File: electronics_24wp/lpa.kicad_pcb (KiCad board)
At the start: 2 copper layers, 143 x 74 mm, 89 parts, among them IC1 ATMEGA328-A, P1 CONN_2, P2 CONN_3X2, U1 SD_CARD, U2 LD1117S33, U3 TLC5941, U4 TLC5941, U5 TLC5941, X1 CRYSTAL_SMD

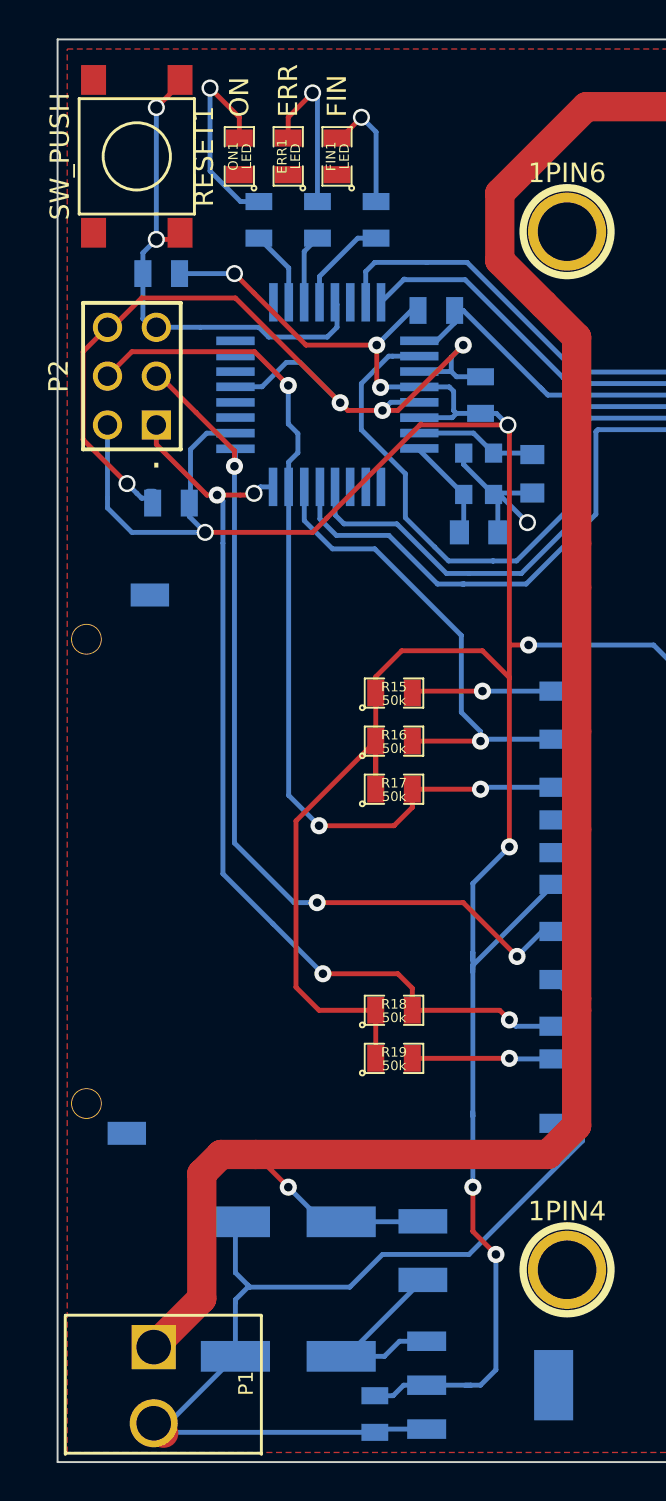
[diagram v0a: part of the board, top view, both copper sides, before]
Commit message: Streamlined layout libraries.
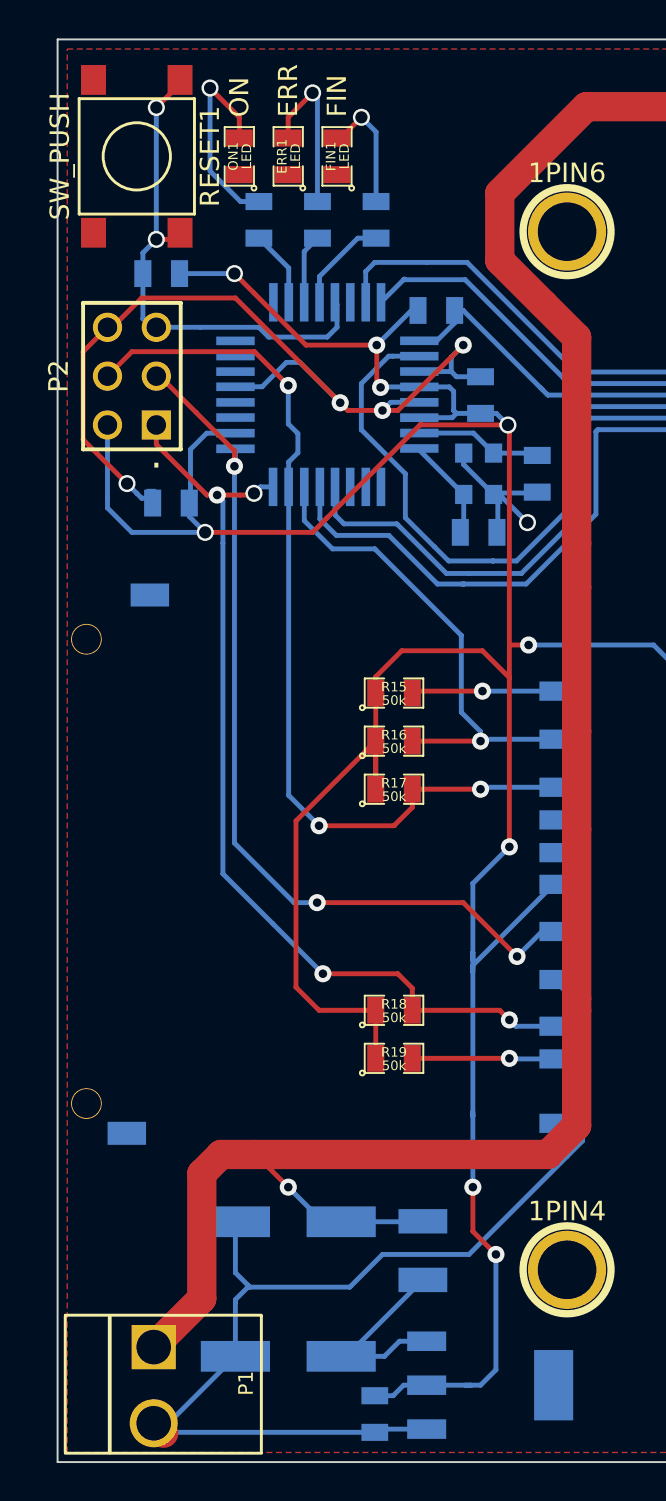
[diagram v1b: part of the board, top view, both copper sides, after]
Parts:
- C1, C2, C5, C6, C7, C8, ERR1, FIN1, ON1, R1, R15, R16, R17, R18, R19, R2, R3, R4, R5, R_ERR1, R_FIN1, R_ON1: footprint SM0805 -> LPA_parts:SM0805
- C10, C9: footprint Capacitors_SMD:C_0805 -> LPA_parts:SM0805
- D1, D10, D11, D12, D13, D14, D15, D16, D17, D18, D19, D2, D20, D21, D22, D23, D24, D25, D26, D27, D28, D29, D3, D30, D31, D32, D33, D34, D35, D36, D37, D38, D39, D4, D40, D41, D42, D43, D44, D45, D46, D47, D48, D5, D6, D7, D8, D9: footprint LPA_parts:PCV220_LEDSOCKET -> LPA_parts:PCV220_LED_SOCKET
- IC1: footprint TQFP32_FIXED -> LPA_parts:ATMEGA328
- P1: footprint PIN_ARRAY_2X1_3960um -> LPA_parts:CONNECTOR_2X1_3960um
- RESET1: footprint SW_PUSH_SMD -> LPA_parts:SW_PUSH_SMD
- U1: footprint SD_CONN -> LPA_parts:SD_CARD_SOCKET
- U3, U4, U5: footprint LPA_parts:TLC5940_THERMVIAS -> LPA_parts:TLC5941
- X1: footprint LPA_parts:Crystal_SMD_3.2_2.5_4pins -> LPA_parts:CRYSTAL_SMD_3.2_2.5_4pins
- moved C9 0.25 mm to (91.9, 117.1)

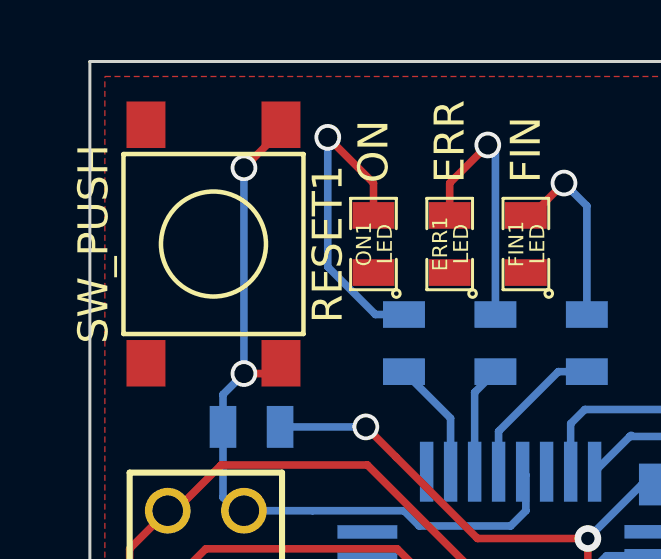
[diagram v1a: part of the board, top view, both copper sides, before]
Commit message: Changed reset button layout for standard library item.
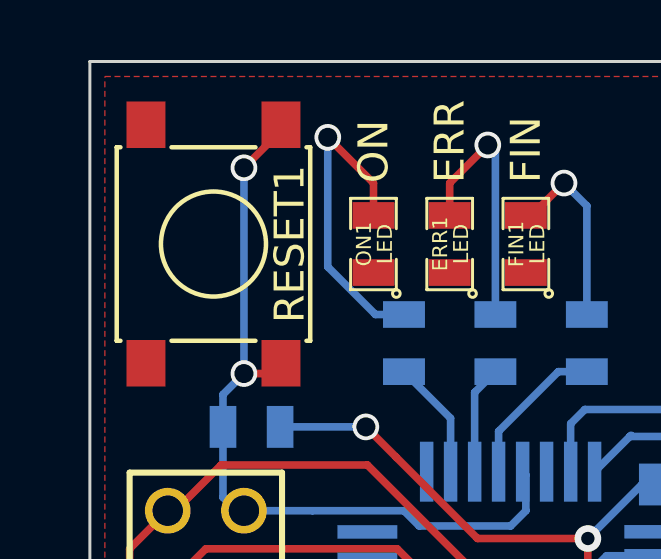
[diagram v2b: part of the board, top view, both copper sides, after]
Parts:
- RESET1: footprint LPA_parts:SW_PUSH_SMD -> Buttons_Switches_SMD:SW_SPST_PTS645
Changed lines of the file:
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@@
     (pad H thru_hole circle (at 0 -12.85 180) (size 1.6 1.6) (drill 1.5) (layers *.Cu *.Mask B.SilkS))
-  )
-  (module LPA_parts:SW_PUSH_SMD (layer F.Cu)
-    (at 71.12 100.584 270)
-    (fp_text reference RESET1 (at 0 -3.81 270) (layer F.SilkS)
-      (effects (font (size 1 1) (thickness 0.15)))
-    )
-    (fp_text value SW_PUSH (at 0 4 270) (layer F.SilkS)
-      (effects (font (size 1 1) (thickness 0.15)))
-    )
-    (fp_circle (center 0 0) (end 1.75 0) (layer F.SilkS) (width 0.15))
-    (fp_line (start -3 -3) (end -3 3) (layer F.SilkS) (width 0.15))
-    (fp_line (start -3 3) (end 3 3) (layer F.SilkS) (width 0.15))
-    (fp_line (start 3 3) (end 3 -3) (layer F.SilkS) (width 0.15))
-    (fp_line (start 3 -3) (end -3 -3) (layer F.SilkS) (width 0.15))
-    (pad 1 smd rect (at 3.975 -2.25 270) (size 1.55 1.3) (layers F.Cu F.Paste F.Mask)
-      (net 6 /RST))
-    (pad 2 smd rect (at 3.975 2.25 270) (size 1.55 1.3) (layers F.Cu F.Paste F.Mask)
-      (net 17 GND))
-    (pad 2 smd rect (at -3.975 2.25 270) (size 1.55 1.3) (layers F.Cu F.Paste F.Mask)
-      (net 17 GND))
-    (pad 1 smd rect (at -3.975 -2.25 270) (size 1.55 1.3) (layers F.Cu F.Paste F.Mask)
-      (net 6 /RST))
   )
   (module LPA_parts:CONNECTOR_2X1_3960um (layer F.Cu)
@@
     )
   )
+  (module Buttons_Switches_SMD:SW_SPST_PTS645 (layer F.Cu)
+    (at 71.12 100.584 270)
+    (descr "C&K Components SPST SMD PTS645 Series 6mm Tact Switch")
+    (tags "SPST Button Switch")
+    (fp_text reference RESET1 (at 0 -2.54 270) (layer F.SilkS)
+      (effects (font (size 1 1) (thickness 0.15)))
+    )
+    (fp_text value SW_PUSH (at 0 4.064 270) (layer F.Fab)
+      (effects (font (size 1 1) (thickness 0.15)))
+    )
+    (fp_circle (center 0 0) (end 1.75 -0.05) (layer F.SilkS) (width 0.15))
+    (fp_line (start 5.05 3.4) (end 5.05 -3.4) (layer F.CrtYd) (width 0.05))
+    (fp_line (start -5.05 -3.4) (end -5.05 3.4) (layer F.CrtYd) (width 0.05))
+    (fp_line (start -5.05 3.4) (end 5.05 3.4) (layer F.CrtYd) (width 0.05))
+    (fp_line (start -5.05 -3.4) (end 5.05 -3.4) (layer F.CrtYd) (width 0.05))
+    (fp_line (start 3.225 -3.225) (end 3.225 -3.1) (layer F.SilkS) (width 0.15))
+    (fp_line (start 3.225 3.225) (end 3.225 3.1) (layer F.SilkS) (width 0.15))
+    (fp_line (start -3.225 3.225) (end -3.225 3.1) (layer F.SilkS) (width 0.15))
+    (fp_line (start -3.225 -3.1) (end -3.225 -3.225) (layer F.SilkS) (width 0.15))
+    (fp_line (start 3.225 -1.4) (end 3.225 1.4) (layer F.SilkS) (width 0.15))
+    (fp_line (start -3.225 -3.225) (end 3.225 -3.225) (layer F.SilkS) (width 0.15))
+    (fp_line (start -3.225 -1.4) (end -3.225 1.4) (layer F.SilkS) (width 0.15))
+    (fp_line (start -3.225 3.225) (end 3.225 3.225) (layer F.SilkS) (width 0.15))
+    (pad 2 smd rect (at -3.975 2.25 270) (size 1.55 1.3) (layers F.Cu F.Paste F.Mask)
+      (net 17 GND))
+    (pad 1 smd rect (at -3.975 -2.25 270) (size 1.55 1.3) (layers F.Cu F.Paste F.Mask)
+      (net 6 /RST))
+    (pad 1 smd rect (at 3.975 -2.25 270) (size 1.55 1.3) (layers F.Cu F.Paste F.Mask)
+      (net 6 /RST))
+    (pad 2 smd rect (at 3.975 2.25 270) (size 1.55 1.3) (layers F.Cu F.Paste F.Mask)
+      (net 17 GND))
+  )
   (gr_text . (at 72.136 116.078) (layer F.SilkS)

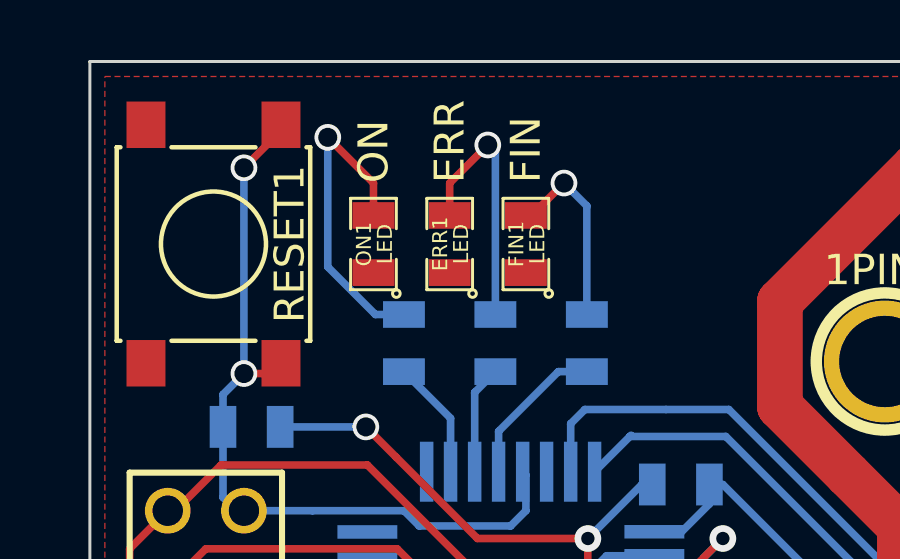
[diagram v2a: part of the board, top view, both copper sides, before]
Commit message: Changed orientation of error LED.
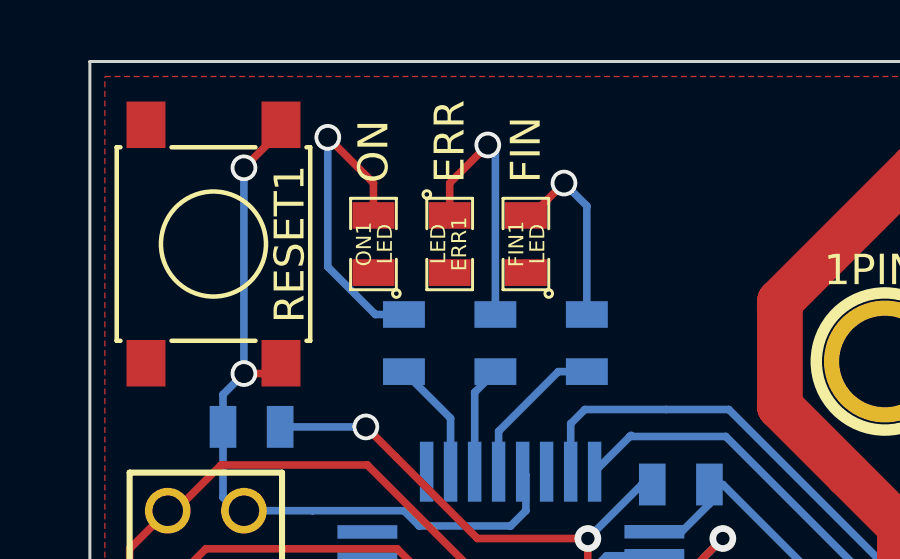
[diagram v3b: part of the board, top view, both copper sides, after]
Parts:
- turned ERR1 to 270 degrees
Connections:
- ERR1 pad 1: GND -> Net-(ERR1-Pad1)
- ERR1 pad 2: Net-(ERR1-Pad2) -> GND
- R_ERR1 pad 2: Net-(ERR1-Pad2) -> Net-(ERR1-Pad1)
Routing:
- net Net-(ERR1-Pad2): track 8.63 -> 0.00 mm, vias 1 -> 0
- net Net-(ERR1-Pad1): track 0.00 -> 8.63 mm, vias 0 -> 1
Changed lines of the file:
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@@
   (net 88 "Net-(U5-Pad23)")
   (net 89 "Net-(U5-Pad24)")
-  (net 90 "Net-(ERR1-Pad2)")
-  (net 91 "Net-(FIN1-Pad2)")
-  (net 92 "Net-(ON1-Pad2)")
+  (net 90 "Net-(FIN1-Pad2)")
+  (net 91 "Net-(ON1-Pad2)")
+  (net 92 "Net-(ERR1-Pad1)")
   (net_class Default "This is the default net class."
     (clearance 0.254)
@@
     (add_net "Net-(D8-Pad2)")
     (add_net "Net-(D9-Pad2)")
-    (add_net "Net-(ERR1-Pad2)")
+    (add_net "Net-(ERR1-Pad1)")
     (add_net "Net-(FIN1-Pad2)")
     (add_net "Net-(IC1-Pad10)")
@@
       (net 2 /FIN))
     (pad 2 smd rect (at 0.9525 0 90) (size 0.889 1.397) (layers B.Cu B.Paste B.Mask)
-      (net 91 "Net-(FIN1-Pad2)"))
+      (net 90 "Net-(FIN1-Pad2)"))
     (model smd/chip_cms.wrl
       (at (xyz 0 0 0))
@@
       (net 1 /ERR))
     (pad 2 smd rect (at 0.9525 0 90) (size 0.889 1.397) (layers B.Cu B.Paste B.Mask)
-      (net 90 "Net-(ERR1-Pad2)"))
+      (net 92 "Net-(ERR1-Pad1)"))
     (model smd/chip_cms.wrl
       (at (xyz 0 0 0))
@@
       (net 5 /ON))
     (pad 2 smd rect (at 0.9525 0 90) (size 0.889 1.397) (layers B.Cu B.Paste B.Mask)
-      (net 92 "Net-(ON1-Pad2)"))
+      (net 91 "Net-(ON1-Pad2)"))
     (model smd/chip_cms.wrl
       (at (xyz 0 0 0))
@@
       (net 17 GND))
     (pad 2 smd rect (at 0.9525 0 90) (size 0.889 1.397) (layers F.Cu F.Paste F.Mask)
-      (net 91 "Net-(FIN1-Pad2)"))
+      (net 90 "Net-(FIN1-Pad2)"))
     (model smd/chip_cms.wrl
       (at (xyz 0 0 0))
@@
   )
   (module LPA_parts:SM0805 (layer F.Cu)
-    (at 78.994 100.584 90)
+    (at 78.994 100.584 270)
     (attr smd)
-    (fp_text reference ERR1 (at 0 -0.3175 90) (layer F.SilkS)
+    (fp_text reference ERR1 (at 0 -0.3175 270) (layer F.SilkS)
       (effects (font (size 0.50038 0.50038) (thickness 0.10922)))
     )
-    (fp_text value LED (at 0 0.381 90) (layer F.SilkS)
+    (fp_text value LED (at 0 0.381 270) (layer F.SilkS)
       (effects (font (size 0.50038 0.50038) (thickness 0.10922)))
     )
@@
     (fp_line (start 1.524 -0.762) (end 1.524 0.762) (layer F.SilkS) (width 0.09906))
     (fp_line (start 1.524 0.762) (end 0.508 0.762) (layer F.SilkS) (width 0.09906))
-    (pad 1 smd rect (at -0.9525 0 90) (size 0.889 1.397) (layers F.Cu F.Paste F.Mask)
+    (pad 1 smd rect (at -0.9525 0 270) (size 0.889 1.397) (layers F.Cu F.Paste F.Mask)
+      (net 92 "Net-(ERR1-Pad1)"))
+    (pad 2 smd rect (at 0.9525 0 270) (size 0.889 1.397) (layers F.Cu F.Paste F.Mask)
       (net 17 GND))
-    (pad 2 smd rect (at 0.9525 0 90) (size 0.889 1.397) (layers F.Cu F.Paste F.Mask)
-      (net 90 "Net-(ERR1-Pad2)"))
     (model smd/chip_cms.wrl
       (at (xyz 0 0 0))
@@
       (net 17 GND))
     (pad 2 smd rect (at 0.9525 0 90) (size 0.889 1.397) (layers F.Cu F.Paste F.Mask)
-      (net 92 "Net-(ON1-Pad2)"))
+      (net 91 "Net-(ON1-Pad2)"))
     (model smd/chip_cms.wrl
       (at (xyz 0 0 0))
@@
   (via (at 200.3 133.7) (size 0.889) (layers F.Cu B.Cu) (net 89))
   (segment (start 199.7 133.1) (end 200.3 133.7) (width 0.254) (layer F.Cu) (net 89))
-  (segment (start 78.994 98.552) (end 78.994 99.6315) (width 0.254) (layer F.Cu) (net 90))
-  (segment (start 80.264 97.282) (end 78.994 98.552) (width 0.254) (layer F.Cu) (net 90))
-  (via (at 80.264 97.282) (size 0.889) (drill 0.635) (layers F.Cu B.Cu) (net 90))
-  (segment (start 80.518 97.536) (end 80.264 97.282) (width 0.254) (layer B.Cu) (net 90))
-  (segment (start 80.518 102.9335) (end 80.518 97.536) (width 0.254) (layer B.Cu) (net 90))
-  (segment (start 82.804 98.552) (end 81.7245 99.6315) (width 0.254) (layer F.Cu) (net 91))
-  (via (at 82.804 98.552) (size 0.889) (drill 0.635) (layers F.Cu B.Cu) (net 91))
-  (segment (start 81.7245 99.6315) (end 81.534 99.6315) (width 0.254) (layer F.Cu) (net 91))
-  (segment (start 83.566 99.314) (end 82.804 98.552) (width 0.254) (layer B.Cu) (net 91))
-  (segment (start 83.566 102.9335) (end 83.566 99.314) (width 0.254) (layer B.Cu) (net 91))
-  (segment (start 83.566 102.9335) (end 83.566 102.87) (width 0.254) (layer B.Cu) (net 91))
-  (segment (start 76.454 98.552) (end 76.454 99.6315) (width 0.254) (layer F.Cu) (net 92))
-  (segment (start 74.93 97.028) (end 76.454 98.552) (width 0.254) (layer F.Cu) (net 92))
-  (segment (start 77.47 102.9335) (end 76.5175 102.9335) (width 0.254) (layer B.Cu) (net 92))
-  (segment (start 76.5175 102.9335) (end 74.93 101.346) (width 0.254) (layer B.Cu) (net 92))
-  (segment (start 74.93 101.346) (end 74.93 97.028) (width 0.254) (layer B.Cu) (net 92))
-  (via (at 74.93 97.028) (size 0.889) (drill 0.635) (layers F.Cu B.Cu) (net 92))
+  (segment (start 82.804 98.552) (end 81.7245 99.6315) (width 0.254) (layer F.Cu) (net 90))
+  (via (at 82.804 98.552) (size 0.889) (drill 0.635) (layers F.Cu B.Cu) (net 90))
+  (segment (start 81.7245 99.6315) (end 81.534 99.6315) (width 0.254) (layer F.Cu) (net 90))
+  (segment (start 83.566 99.314) (end 82.804 98.552) (width 0.254) (layer B.Cu) (net 90))
+  (segment (start 83.566 102.9335) (end 83.566 99.314) (width 0.254) (layer B.Cu) (net 90))
+  (segment (start 83.566 102.9335) (end 83.566 102.87) (width 0.254) (layer B.Cu) (net 90))
+  (segment (start 76.454 98.552) (end 76.454 99.6315) (width 0.254) (layer F.Cu) (net 91))
+  (segment (start 74.93 97.028) (end 76.454 98.552) (width 0.254) (layer F.Cu) (net 91))
+  (segment (start 77.47 102.9335) (end 76.5175 102.9335) (width 0.254) (layer B.Cu) (net 91))
+  (segment (start 76.5175 102.9335) (end 74.93 101.346) (width 0.254) (layer B.Cu) (net 91))
+  (segment (start 74.93 101.346) (end 74.93 97.028) (width 0.254) (layer B.Cu) (net 91))
+  (via (at 74.93 97.028) (size 0.889) (drill 0.635) (layers F.Cu B.Cu) (net 91))
+  (segment (start 78.994 98.552) (end 78.994 99.6315) (width 0.254) (layer F.Cu) (net 92))
+  (segment (start 80.264 97.282) (end 78.994 98.552) (width 0.254) (layer F.Cu) (net 92))
+  (via (at 80.264 97.282) (size 0.889) (drill 0.635) (layers F.Cu B.Cu) (net 92))
+  (segment (start 80.518 97.536) (end 80.264 97.282) (width 0.254) (layer B.Cu) (net 92))
+  (segment (start 80.518 102.9335) (end 80.518 97.536) (width 0.254) (layer B.Cu) (net 92))
   (zone (net 17) (net_name GND) (layer F.Cu) (hatch edge 0.508)
     (connect_pads yes (clearance 0.508))
